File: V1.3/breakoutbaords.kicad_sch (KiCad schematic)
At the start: 10 parts, among them J13 USB_A, J3 Conn_02x19_Top_Bottom, J4 Conn_02x19_Top_Bottom, U3 AMS1117-3.3

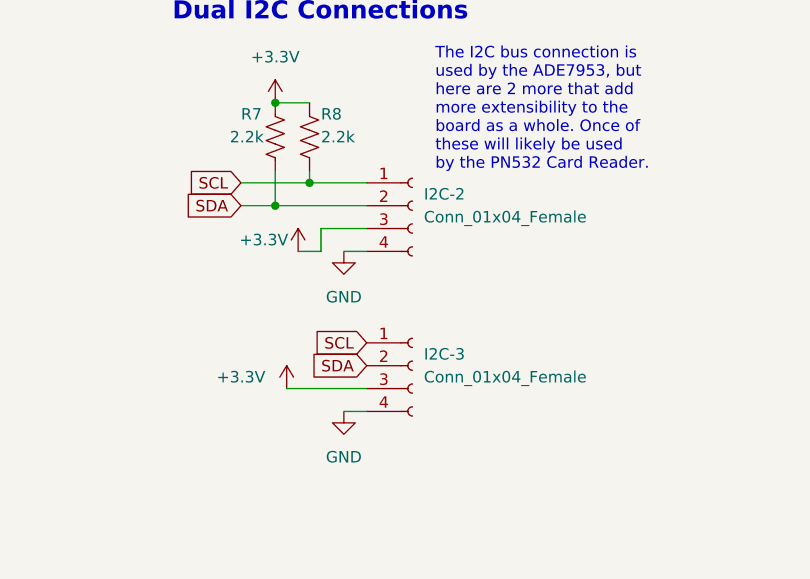
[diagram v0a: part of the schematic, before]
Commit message: fix(breakoutboards): flipped I2C pins, to conform with common wire colors [on JST connectors]
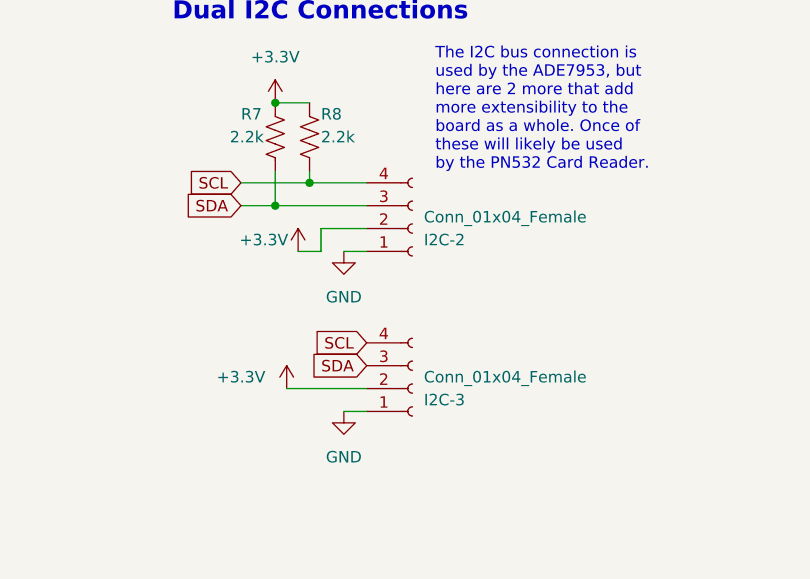
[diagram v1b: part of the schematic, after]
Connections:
- net +3.3V: now also I2C-2.2 (Pin_2), I2C-3.2 (Pin_2); no longer I2C-2.3 (Pin_3), I2C-3.3 (Pin_3)
- net GND: now also I2C-2.1 (Pin_1), I2C-3.1 (Pin_1); no longer I2C-2.4 (Pin_4), I2C-3.4 (Pin_4)
- net SCL: now also I2C-2.4 (Pin_4), I2C-3.4 (Pin_4); no longer I2C-2.1 (Pin_1), I2C-3.1 (Pin_1)
- net SDA: now also I2C-2.3 (Pin_3), I2C-3.3 (Pin_3); no longer I2C-2.2 (Pin_2), I2C-3.2 (Pin_2)
